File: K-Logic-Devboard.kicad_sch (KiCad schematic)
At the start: 25 parts, among them J1 USB_C_Receptacle_USB2.0_14P, U1 RP2040, U2 NCP1117-3.3_SOT223, Y1 12 Mhz

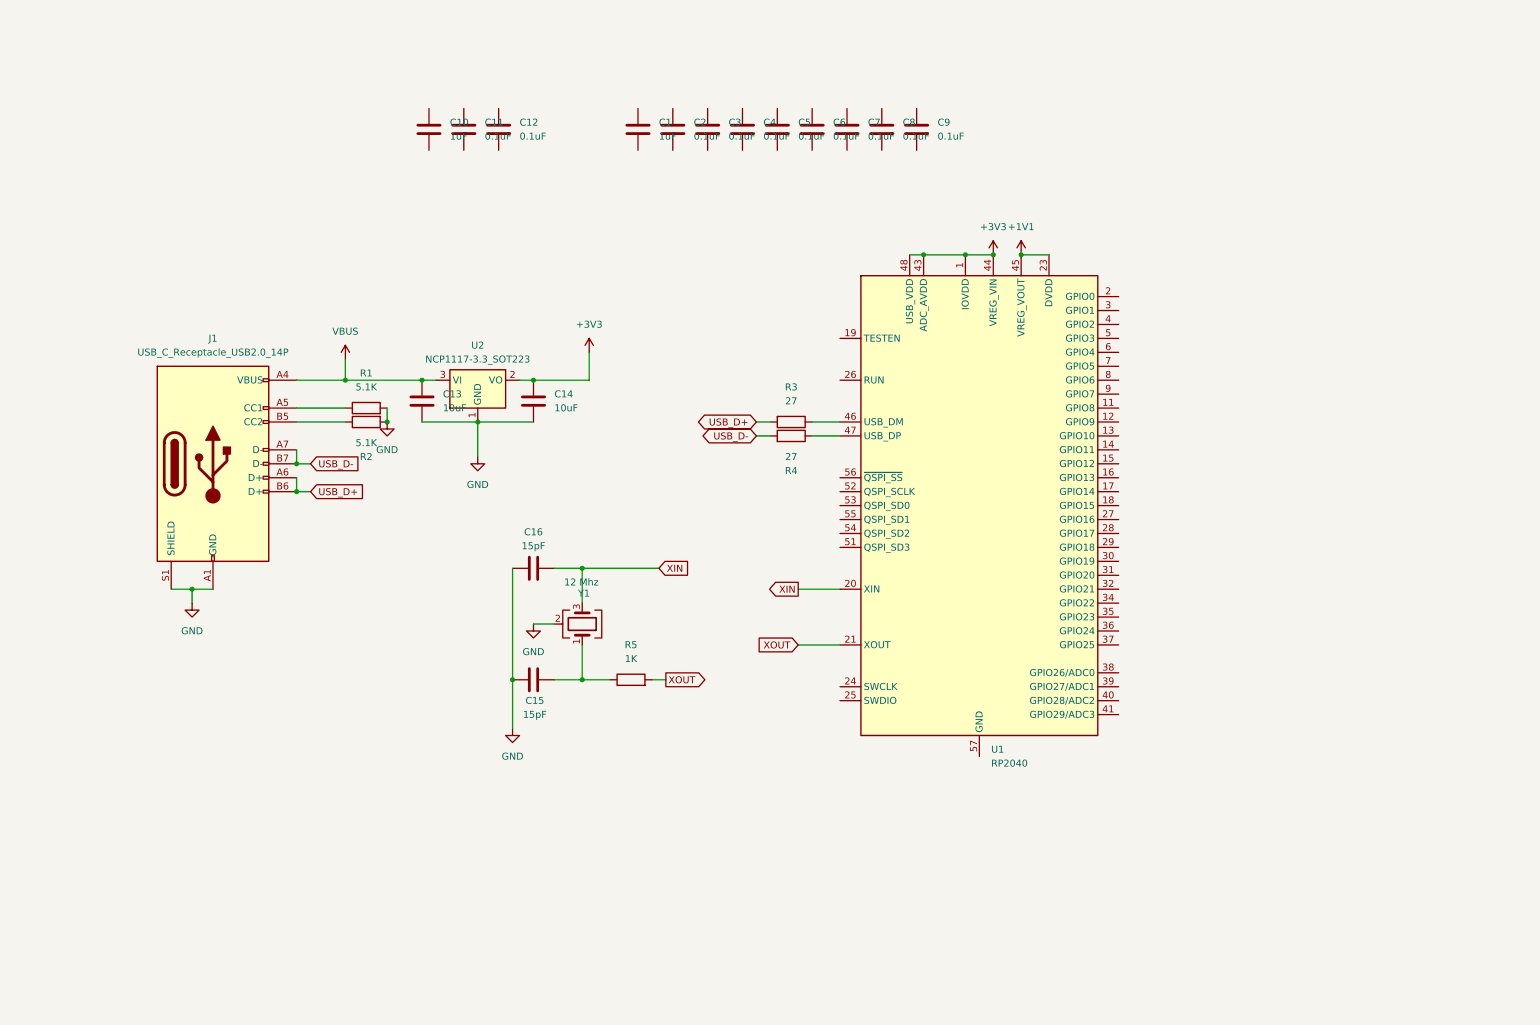
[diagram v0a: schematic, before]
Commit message: worked on flash storage, i/o headers and footprints
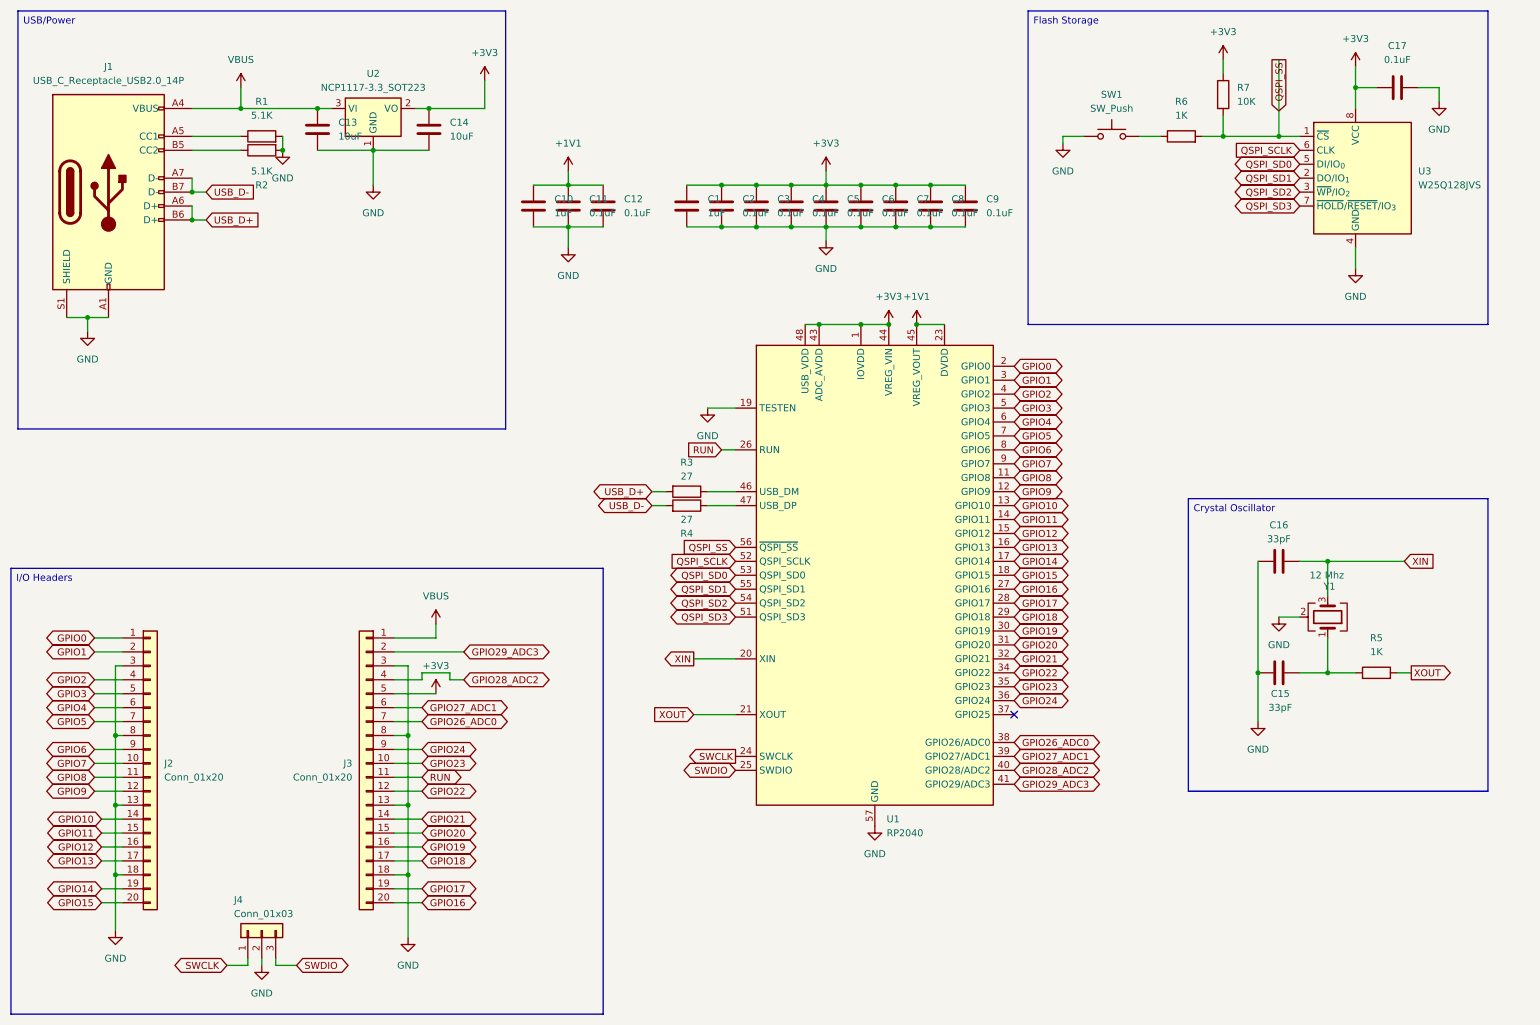
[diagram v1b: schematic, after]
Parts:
- added C17: 0.1uF, Capacitor_SMD:C_0402_1005Metric, symbol Device:C
- added J2, J3: Conn_01x20, Connector_PinHeader_2.54mm:PinHeader_1x20_P2.54mm_Vertical, symbol Connector_Generic:Conn_01x20
- added J4: Conn_01x03, Connector_PinHeader_2.54mm:PinHeader_1x03_P2.54mm_Vertical, symbol Connector_Generic:Conn_01x03
- added R6: 1K, Resistor_SMD:R_0402_1005Metric, symbol Device:R
- added R7: 10K, Resistor_SMD:R_0402_1005Metric, symbol Device:R
- added SW1: SW_Push, Button_Switch_SMD:SW_Push_SPST_NO_Alps_SKRK, symbol Switch:SW_Push
- added U3: W25Q128JVS, Package_SO:SOIC-8_5.3x5.3mm_P1.27mm, symbol Memory_Flash:W25Q128JVS
- C1, C10, C11, C12, C2, C3, C4, C5, C6, C7, C8, C9: footprint (none) -> Capacitor_SMD:C_0402_1005Metric
- C13, C14: footprint (none) -> Capacitor_SMD:C_0603_1608Metric
- C15, C16: value 15pF -> 33pF; footprint (none) -> Capacitor_SMD:C_0402_1005Metric
- J1: footprint (none) -> Connector_USB:USB_C_Receptacle_HRO_TYPE-C-31-M-12
- R1, R2, R3, R4, R5: footprint (none) -> Resistor_SMD:R_0402_1005Metric
- Y1: footprint (none) -> Crystal:Crystal_SMD_3225-4Pin_3.2x2.5mm
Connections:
- net +1V1: now also C10.1, C11.1, C12.1
- net +3V3: now also C1.1, C2.1, C3.1, C4.1, C5.1, C6.1, C7.1, C8.1, C9.1, C17.2, J3.5 (Pin_5), R7.1, U3.8 (VCC)
- net GND: now also C1.2, C10.2, C11.2, C12.2, C2.2, C3.2, C4.2, C5.2, C6.2, C7.2, C8.2, C9.2, U1.19 (TESTEN), U1.57 (GND), C17.1, J2.13 (Pin_13), J2.18 (Pin_18), J2.3 (Pin_3), J2.8 (Pin_8), J3.13 (Pin_13), J3.18 (Pin_18), J3.3 (Pin_3), J3.8 (Pin_8), J4.2 (Pin_2), SW1.1, U3.4 (GND)
- net VBUS: now also J3.1 (Pin_1)
- net GPIO8: now reaches U1.11 (GPIO8)
- net GPIO8: now also J2.11 (Pin_11)
- net GPIO9: now reaches U1.12 (GPIO9)
- net GPIO9: now also J2.12 (Pin_12)
- net GPIO10: now reaches U1.13 (GPIO10)
- net GPIO10: now also J2.14 (Pin_14)
- net GPIO11: now reaches U1.14 (GPIO11)
- net GPIO11: now also J2.15 (Pin_15)
- net GPIO12: now reaches U1.15 (GPIO12)
- net GPIO12: now also J2.16 (Pin_16)
- net GPIO13: now reaches U1.16 (GPIO13)
- net GPIO13: now also J2.17 (Pin_17)
- net GPIO14: now reaches U1.17 (GPIO14)
- net GPIO14: now also J2.19 (Pin_19)
- net GPIO15: now reaches U1.18 (GPIO15)
- net GPIO15: now also J2.20 (Pin_20)
- net GPIO0: now reaches U1.2 (GPIO0)
- net GPIO0: now also J2.1 (Pin_1)
- net SWCLK: now reaches U1.24 (SWCLK)
- net SWCLK: now also J4.1 (Pin_1)
- net SWDIO: now reaches U1.25 (SWDIO)
- net SWDIO: now also J4.3 (Pin_3)
- net RUN: now reaches U1.26 (RUN)
- net RUN: now also J3.11 (Pin_11)
- net GPIO16: now reaches U1.27 (GPIO16)
- net GPIO16: now also J3.20 (Pin_20)
- net GPIO17: now reaches U1.28 (GPIO17)
- net GPIO17: now also J3.19 (Pin_19)
- net GPIO18: now reaches U1.29 (GPIO18)
- net GPIO18: now also J3.17 (Pin_17)
- net GPIO1: now reaches U1.3 (GPIO1)
- net GPIO1: now also J2.2 (Pin_2)
- net GPIO19: now reaches U1.30 (GPIO19)
- net GPIO19: now also J3.16 (Pin_16)
- net GPIO20: now reaches U1.31 (GPIO20)
- net GPIO20: now also J3.15 (Pin_15)
- net GPIO21: now reaches U1.32 (GPIO21)
- net GPIO21: now also J3.14 (Pin_14)
- net GPIO22: now reaches U1.34 (GPIO22)
- net GPIO22: now also J3.12 (Pin_12)
- net GPIO23: now reaches U1.35 (GPIO23)
- net GPIO23: now also J3.10 (Pin_10)
- net GPIO24: now reaches U1.36 (GPIO24)
- net GPIO24: now also J3.9 (Pin_9)
- net GPIO26_ADC0: now reaches U1.38 (GPIO26/ADC0)
- net GPIO26_ADC0: now also J3.7 (Pin_7)
- net GPIO27_ADC1: now reaches U1.39 (GPIO27/ADC1)
- net GPIO27_ADC1: now also J3.6 (Pin_6)
- net GPIO2: now reaches U1.4 (GPIO2)
- net GPIO2: now also J2.4 (Pin_4)
- net GPIO28_ADC2: now reaches U1.40 (GPIO28/ADC2)
- net GPIO28_ADC2: now also J3.4 (Pin_4)
- net GPIO29_ADC3: now reaches U1.41 (GPIO29/ADC3)
- net GPIO29_ADC3: now also J3.2 (Pin_2)
- net GPIO3: now reaches U1.5 (GPIO3)
- net GPIO3: now also J2.5 (Pin_5)
- net QSPI_SD3: now reaches U1.51 (QSPI_SD3)
- net QSPI_SD3: now also U3.7 (~{HOLD}/~{RESET}/IO_{3})
- net QSPI_SCLK: now reaches U1.52 (QSPI_SCLK)
- net QSPI_SCLK: now also U3.6 (CLK)
- net QSPI_SD0: now reaches U1.53 (QSPI_SD0)
- net QSPI_SD0: now also U3.5 (DI/IO_{0})
- net QSPI_SD2: now reaches U1.54 (QSPI_SD2)
- net QSPI_SD2: now also U3.3 (~{WP}/IO_{2})
- net QSPI_SD1: now reaches U1.55 (QSPI_SD1)
- net QSPI_SD1: now also U3.2 (DO/IO_{1})
- net QSPI_SS: now reaches U1.56 (~{QSPI_SS})
- net QSPI_SS: now also R6.2, R7.2, U3.1 (~{CS})
- net GPIO4: now reaches U1.6 (GPIO4)
- net GPIO4: now also J2.6 (Pin_6)
- net GPIO5: now reaches U1.7 (GPIO5)
- net GPIO5: now also J2.7 (Pin_7)
- net GPIO6: now reaches U1.8 (GPIO6)
- net GPIO6: now also J2.9 (Pin_9)
- net GPIO7: now reaches U1.9 (GPIO7)
- net GPIO7: now also J2.10 (Pin_10)
- new net: R6.1, SW1.2
- no-connect marks 0 -> 1
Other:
- moved on the sheet: C1, C10, C11, C12, C13, C14, C15, C16, C2, C3, C4, C5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

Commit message: third session: worked on the pcb design
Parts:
- removed U2: NCP1117-3.3_SOT223, Package_TO_SOT_SMD:SOT-223-3_TabPin2, symbol Regulator_Linear:NCP1117-3.3_SOT223
- added U2: MCP1700x-330xxTT, Package_TO_SOT_SMD:SOT-23-3, symbol Regulator_Linear:MCP1700x-330xxTT
- U3: value W25Q128JVS -> W25Q16JVZPIQ TR; footprint Package_SO:SOIC-8_5.3x5.3mm_P1.27mm -> Package_SON:Winbond_USON-8-1EP_3x2mm_P0.5mm_EP0.2x1.6mm
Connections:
- net +3V3: now also U2.2 (VO)
- net GND: now also U2.1 (GND)
- net VBUS: now also U2.3 (VI)
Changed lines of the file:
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@@
 			)
 		)
-		(property "Value" "W25Q128JVS"
+		(property "Value" "W25Q16JVZPIQ TR"
 			(at 269.24 45.7199 0)
 			(effects
@@
 			)
 		)
-		(property "Footprint" "Package_SO:SOIC-8_5.3x5.3mm_P1.27mm"
+		(property "Footprint" "Package_SON:Winbond_USON-8-1EP_3x2mm_P0.5mm_EP0.2x1.6mm"
 			(at 257.81 21.59 0)
 			(effects
@@
 			)
 		)
-		(property "Datasheet" "https://www.winbond.com/resource-files/w25q128jv_dtr%20revc%2003272018%20plus.pdf"
+		(property "Datasheet" ""
 			(at 257.81 19.05 0)
 			(effects
@@
 			)
 		)
-		(property "Description" "128Mbit / 16MiB Serial Flash Memory, Standard/Dual/Quad SPI, 2.7-3.6V, SOIC-8"
+		(property "Description" ""
 			(at 257.81 16.51 0)
 			(effects
@@
 	)
 	(symbol
-		(lib_id "Regulator_Linear:NCP1117-3.3_SOT223")
-		(at 78.74 31.75 0)
-		(unit 1)
-		(exclude_from_sim no)
-		(in_bom yes)
-		(on_board yes)
-		(dnp no)
-		(fields_autoplaced yes)
-		(property "Reference" "U2"
-			(at 78.74 25.4 0)
-			(effects
-				(font
-					(size 1.27 1.27)
-				)
-			)
-		)
-		(property "Value" "NCP1117-3.3_SOT223"
-			(at 78.74 27.94 0)
-			(effects
-				(font
-					(size 1.27 1.27)
-				)
-			)
-		)
-		(property "Footprint" "Package_TO_SOT_SMD:SOT-223-3_TabPin2"
-			(at 78.74 26.67 0)
-			(effects
-				(font
-					(size 1.27 1.27)
-				)
-				(hide yes)
-			)
-		)
-		(property "Datasheet" "http://www.onsemi.com/pub_link/Collateral/NCP1117-D.PDF"
-			(at 81.28 38.1 0)
-			(effects
-				(font
-					(size 1.27 1.27)
-				)
-				(hide yes)
-			)
-		)
-		(property "Description" "1A Low drop-out regulator, Fixed Output 3.3V, SOT-223"
-			(at 78.74 31.75 0)
-			(effects
-				(font
-					(size 1.27 1.27)
-				)
-				(hide yes)
-			)
-		)
-		(pin "3"
-		)
-		(pin "1"
-		)
-		(pin "2"
-		)
-		(instances
-			(project ""
-				(path "/73a164d0-d5be-4090-91fb-c8d308b8985d"
-					(reference "U2")
-					(unit 1)
-				)
-			)
-		)
-	)
-	(symbol
 		(lib_id "power:+3V3")
 		(at 99.06 26.67 0)
@@
 					(unit 1)
 				)
+			)
+		)
+	)
+	(symbol
+		(lib_id "Regulator_Linear:MCP1700x-330xxTT")
+		(at 78.74 31.75 0)
+		(unit 1)
+		(exclude_from_sim no)
+		(in_bom yes)
+		(on_board yes)
+		(dnp no)
+		(fields_autoplaced yes)
+		(property "Reference" "U2"
+			(at 78.74 25.4 0)
+			(effects
+				(font
+					(size 1.27 1.27)
+				)
+			)
+		)
+		(property "Value" "MCP1700x-330xxTT"
+			(at 78.74 27.94 0)
+			(effects
+				(font
+					(size 1.27 1.27)
+				)
+			)
+		)
+		(property "Footprint" "Package_TO_SOT_SMD:SOT-23-3"
+			(at 78.74 26.035 0)
+			(effects
+				(font
+					(size 1.27 1.27)
+				)
+				(hide yes)
+			)
+		)
+		(property "Datasheet" "http://ww1.microchip.com/downloads/en/DeviceDoc/20001826D.pdf"
+			(at 78.74 31.75 0)
+			(effects
+				(font
+					(size 1.27 1.27)
+				)
+				(hide yes)
+			)
+		)
+		(property "Description" "250mA Low Quiscent Current LDO, 3.3V output, SOT-23"
+			(at 78.74 31.75 0)
+			(effects
+				(font
+					(size 1.27 1.27)
+				)
+				(hide yes)
+			)
+		)
+		(pin "3"
+		)
+		(pin "2"
+		)
+		(pin "1"
+		)
+		(instances
+			(project ""
+				(path "/73a164d0-d5be-4090-91fb-c8d308b8985d"
+					(reference "U2")
+					(unit 1)
+				)

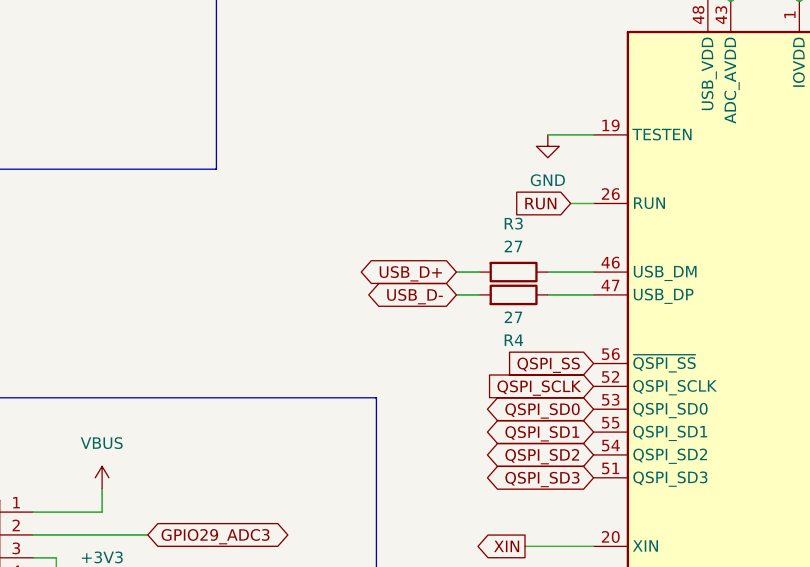
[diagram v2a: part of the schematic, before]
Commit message: pcb 99.99% done. journals and BOM.
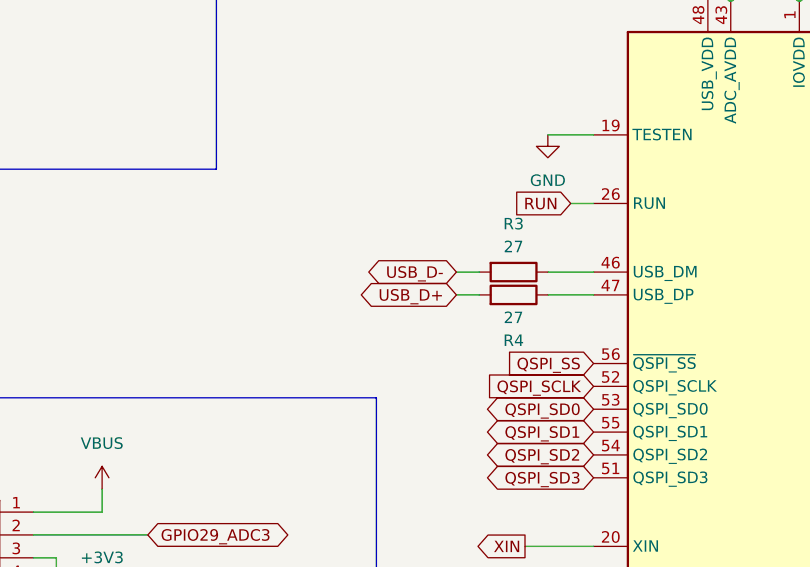
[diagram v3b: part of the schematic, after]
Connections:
- net USB_D+: now also R4.2; no longer R3.2
- net USB_D-: now also R3.2; no longer R4.2
